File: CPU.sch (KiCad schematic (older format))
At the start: 14 parts, among them J101 Conn_02x10_Odd_Even, J102 Conn_02x14_Odd_Even_MountingP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, Q101 IRLML0040TR, Q102 IRLML0040TR, Q103 DMC4050, SW101 SW_SPDT, U101 ATtiny85-20PU

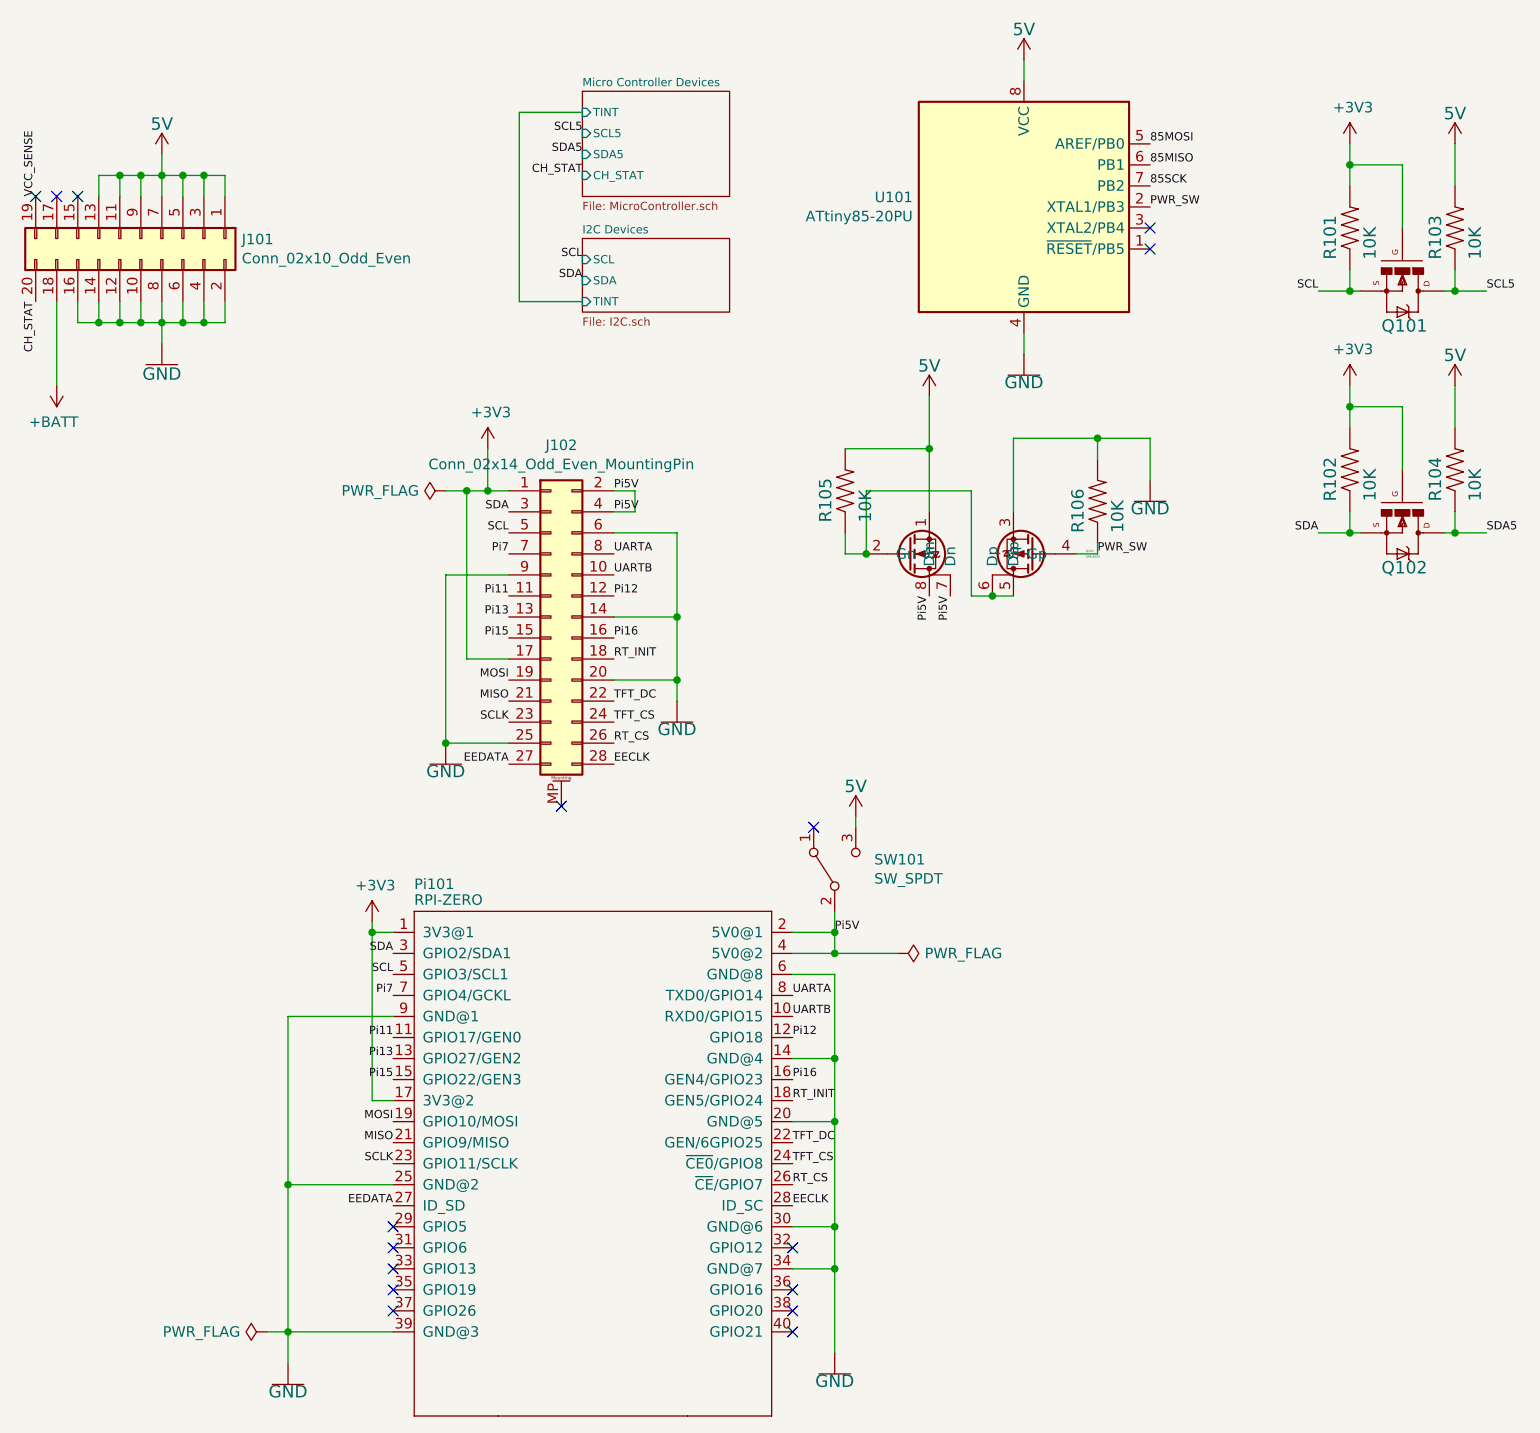
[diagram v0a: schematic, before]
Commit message: Last version before switching to resistive model to read the scroll wheel.
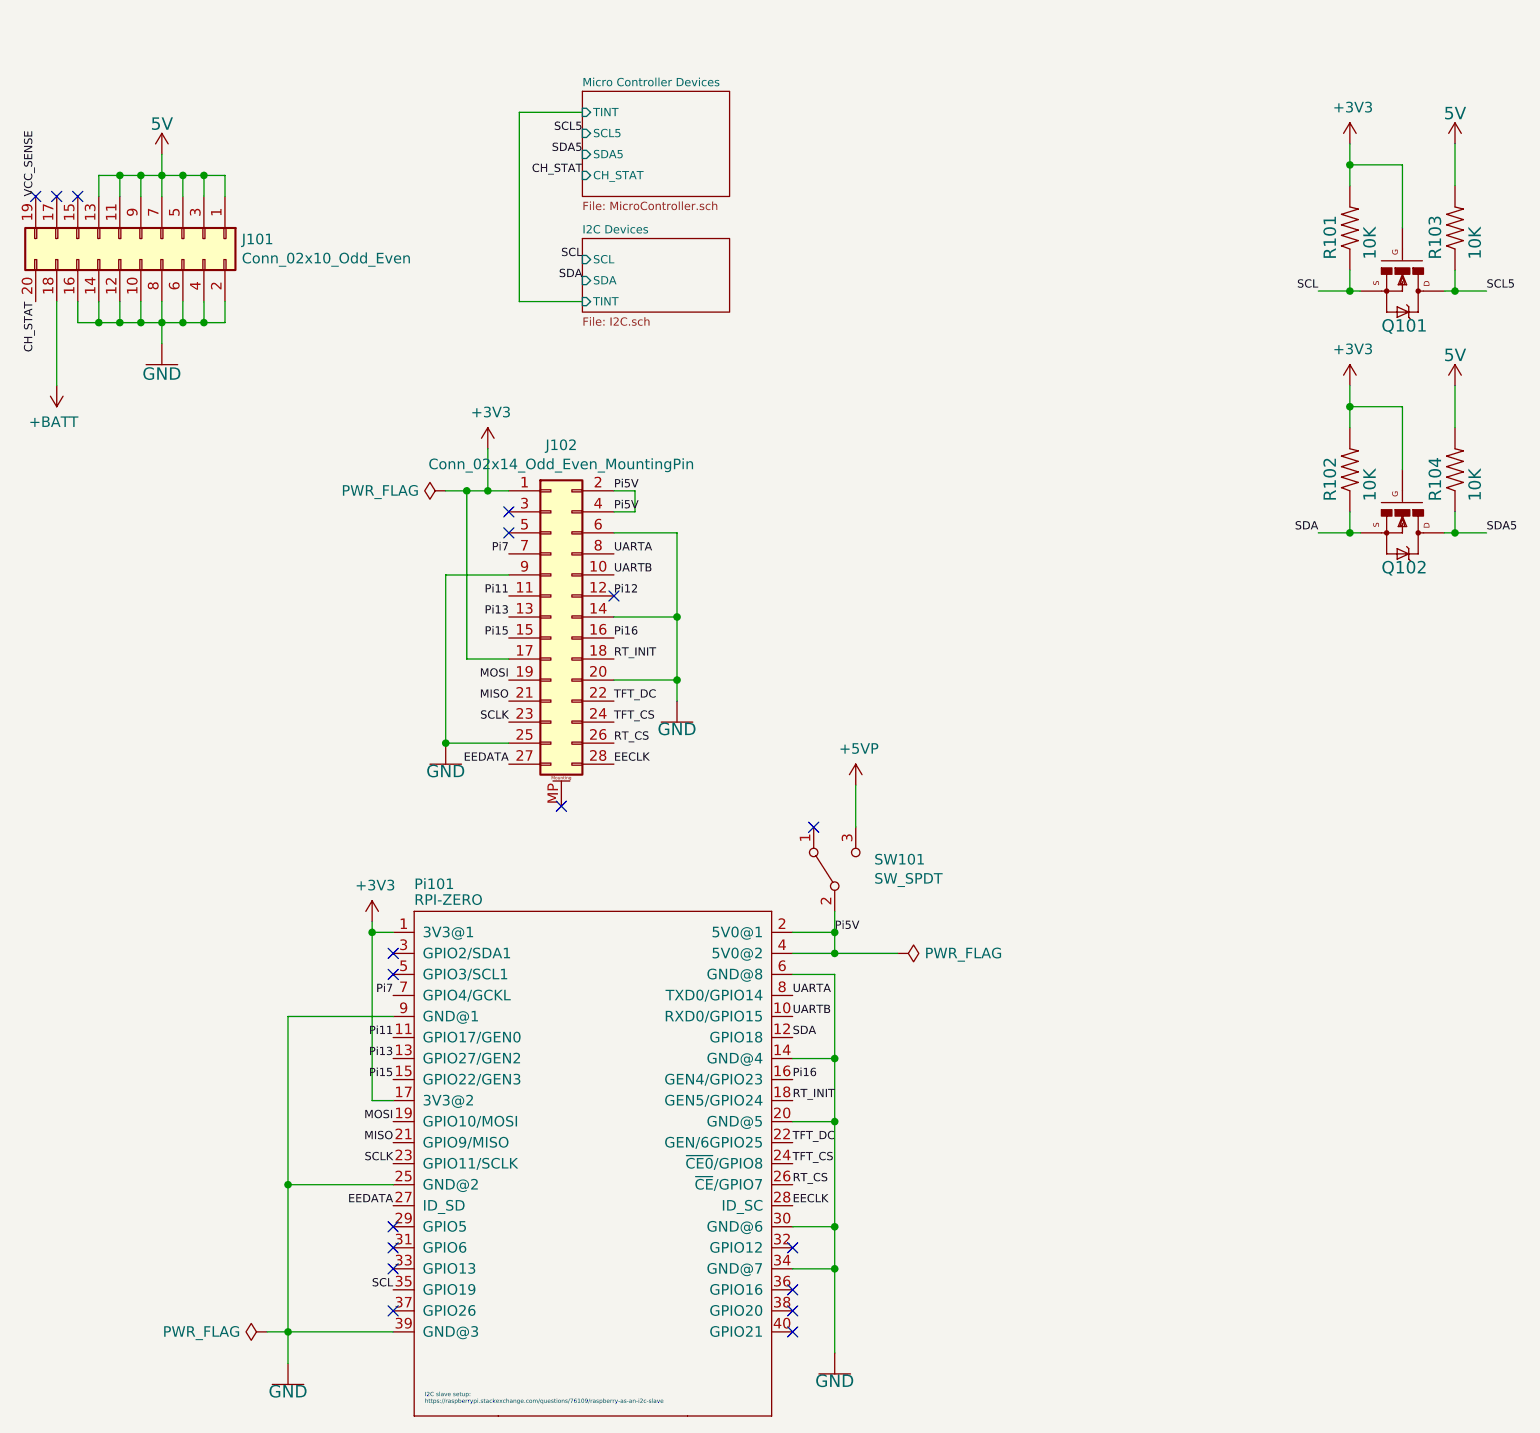
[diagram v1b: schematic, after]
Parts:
- removed Q103: DMC4050, Marco:8-SMD, symbol Marco:DMC4050
- removed R105, R106: 10K, CPU:R1206, symbol CPU-eagle-import:R-US_R1206
- removed U101: ATtiny85-20PU, Marco:8-SMD, symbol MCU_Microchip_ATtiny:ATtiny85-20PU
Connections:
- net Pi12: no longer Pi101.12 (GPIO18)
- net SCL: now also Pi101.35 (GPIO19); no longer J102.5 (Pin_5), Pi101.5 (GPIO3/SCL1)
- net SDA: now also Pi101.12 (GPIO18); no longer J102.3 (Pin_3), Pi101.3 (GPIO2/SDA1)
- net +5VP: now reaches SW101.3 (C)
- no-connect marks 16 -> 18
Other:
- note added: "I2C slave setup:\nhttps://raspberrypi.stackexchange.com/questions/76109/raspberry-as-an-i2c-slave"
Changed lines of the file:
@@
 	5150 5200 5150 5600
 Connection ~ 5150 5600
-$Comp
-L CPU-eagle-import:5V #SUPPLY0102
-U 1 1 5E9EAA7D
-P 5250 4450
-F 0 "#SUPPLY0102" H 5250 4450 50  0001 C CNN
-F 1 "5V" H 5250 4560 59  0000 C BNN
-F 2 "" H 5250 4450 50  0001 C CNN
-F 3 "" H 5250 4450 50  0001 C CNN
-	1    5250 4450
-	1    0    0    -1
-$EndComp
 Wire Wire Line
 	4950 5000 5150 5000
@@
 Text Label 4950 5800 0    39   ~ 0
 RT_INIT
-Text Label 4950 5500 0    39   ~ 0
-Pi12
 $Comp
 L Connector_Generic_MountingPin:Conn_02x14_Odd_Even_MountingPin J102
@@
 	3500 2900 3400 2900
 Connection ~ 3500 2900
-Text Label 3600 3000 2    39   ~ 0
-SDA
-Text Label 3600 3100 2    39   ~ 0
-SCL
 Text Label 3600 3200 2    39   ~ 0
 Pi7
@@
 	5150 5000 5150 4900
 Connection ~ 5150 5000
-Wire Wire Line
-	5250 4500 5250 4450
 Text Label 5150 5000 0    39   ~ 0
 Pi5V
@@
 NoConn ~ 3050 6500
 NoConn ~ 3050 6600
-NoConn ~ 3050 6700
 NoConn ~ 4950 6700
 NoConn ~ 4950 6500
@@
 Text Label 8250 1950 0    39   ~ 0
 SCL5
-Text Label 3050 5100 2    39   ~ 0
+Text Label 4950 5500 0    39   ~ 0
 SDA
-Text Label 3050 5200 2    39   ~ 0
+Text Label 3050 6700 2    39   ~ 0
 SCL
 NoConn ~ 1350 1500
@@
 F4 "TINT" I L 3950 2000 39
 $EndSheet
-$Comp
-L Marco:DMC4050 Q103
-U 1 1 5E925B34
-P 5800 3200
-F 0 "Q103" H 5256 3186 10  0000 R CNN
-F 1 "DMC4050" H 5256 3213 10  0000 R CNN
-F 2 "Marco:8-SMD" H 5800 3200 10  0001 C CNN
-F 3 "" H 5800 3200 10  0001 C CNN
-F 4 "DMC4050SSD-13" H 5800 3200 50  0001 C CNN "DigiKey"
-	1    5800 3200
-	-1   0    0    1
-$EndComp
-$Comp
-L CPU-eagle-import:R-US_R1206 R?
-U 1 1 5E928908
-P 5200 2900
-AR Path="/5E916134/5E928908" Ref="R?"  Part="1"
-AR Path="/5E928908" Ref="R105"  Part="1"
-F 0 "R105" H 5050 2959 59  0000 L BNN
-F 1 "10K" H 5050 2770 59  0000 L BNN
-F 2 "CPU:R1206" H 5200 2900 50  0001 C CNN
-F 3 "" H 5200 2900 50  0001 C CNN
-F 4 " C17902" H 5200 2900 50  0001 C CNN "LCSC Part Number"
-F 5 "RC1206FR-0710KL" H 5200 2900 50  0001 C CNN "DigiKey"
-	1    5200 2900
-	0    -1   -1   0
-$EndComp
-$Comp
-L CPU-eagle-import:R-US_R1206 R?
-U 1 1 5E92C0F5
-P 6400 2950
-AR Path="/5E916134/5E92C0F5" Ref="R?"  Part="1"
-AR Path="/5E92C0F5" Ref="R106"  Part="1"
-F 0 "R106" H 6250 3009 59  0000 L BNN
-F 1 "10K" H 6250 2820 59  0000 L BNN
-F 2 "CPU:R1206" H 6400 2950 50  0001 C CNN
-F 3 "" H 6400 2950 50  0001 C CNN
-F 4 " C17902" H 6400 2950 50  0001 C CNN "LCSC Part Number"
-F 5 "RC1206FR-0710KL" H 6400 2950 50  0001 C CNN "DigiKey"
-	1    6400 2950
-	0    -1   -1   0
-$EndComp
-$Comp
-L CPU-eagle-import:5V #SUPPLY0105
-U 1 1 5E92CA3A
-P 5600 2450
-F 0 "#SUPPLY0105" H 5600 2450 50  0001 C CNN
-F 1 "5V" H 5600 2560 59  0000 C BNN
-F 2 "" H 5600 2450 50  0001 C CNN
-F 3 "" H 5600 2450 50  0001 C CNN
-	1    5600 2450
-	1    0    0    -1
-$EndComp
-Wire Wire Line
-	5200 2700 5600 2700
-Wire Wire Line
-	5600 2700 5600 2450
-Wire Wire Line
-	5600 2700 5600 3000
-Connection ~ 5600 2700
-Wire Wire Line
-	5200 3100 5200 3200
-Wire Wire Line
-	5200 3200 5300 3200
-Wire Wire Line
-	6000 3000 6000 2650
-Wire Wire Line
-	6000 2650 6400 2650
-Wire Wire Line
-	6400 2650 6400 2750
-Wire Wire Line
-	6400 3150 6400 3200
-Wire Wire Line
-	6400 3200 6300 3200
-Wire Wire Line
-	5300 3200 5300 2900
-Wire Wire Line
-	5300 2900 5800 2900
-Wire Wire Line
-	5800 2900 5800 3400
-Wire Wire Line
-	5800 3400 5900 3400
-Connection ~ 5300 3200
-Wire Wire Line
-	6000 3400 5900 3400
-Connection ~ 5900 3400
-Text Label 5600 3400 3    39   ~ 0
-Pi5V
-Text Label 5700 3400 3    39   ~ 0
-Pi5V
-$Comp
-L CPU-eagle-import:GND #GND0106
-U 1 1 5E942D3F
-P 6650 2950
-F 0 "#GND0106" H 6650 2950 50  0001 C CNN
-F 1 "GND" H 6650 2950 59  0000 C TNN
-F 2 "" H 6650 2950 50  0001 C CNN
-F 3 "" H 6650 2950 50  0001 C CNN
-	1    6650 2950
-	1    0    0    -1
-$EndComp
-Wire Wire Line
-	6400 2650 6650 2650
-Wire Wire Line
-	6650 2650 6650 2850
-Connection ~ 6400 2650
-$Comp
-L MCU_Microchip_ATtiny:ATtiny85-20PU U101
-U 1 1 5E9473CE
-P 6050 1550
-F 0 "U101" H 5521 1596 50  0000 R CNN
-F 1 "ATtiny85-20PU" H 5521 1505 50  0000 R CNN
-F 2 "Marco:8-SMD" H 6050 1550 50  0001 C CIN
-F 3 "http://ww1.microchip.com/downloads/en/DeviceDoc/atmel-2586-avr-8-bit-microcontroller-attiny25-attiny45-attiny85_datasheet.pdf" H 6050 1550 50  0001 C CNN
-F 4 "ATTINY85-20SHR" H 6050 1550 50  0001 C CNN "DigiKey"
-	1    6050 1550
-	1    0    0    -1
-$EndComp
-Text Label 6400 3200 0    39   ~ 0
-PWR_SW
-Text Label 6650 1550 0    39   ~ 0
-PWR_SW
-$Comp
-L CPU-eagle-import:5V #SUPPLY?
-U 1 1 5E95C85A
-P 6050 850
-F 0 "#SUPPLY?" H 6050 850 50  0001 C CNN
-F 1 "5V" H 6050 960 59  0000 C BNN
-F 2 "" H 6050 850 50  0001 C CNN
-F 3 "" H 6050 850 50  0001 C CNN
-	1    6050 850
-	1    0    0    -1
-$EndComp
-$Comp
-L CPU-eagle-import:GND #GND?
-U 1 1 5E95CCF7
-P 6050 2350
-F 0 "#GND?" H 6050 2350 50  0001 C CNN
-F 1 "GND" H 6050 2350 59  0000 C TNN
-F 2 "" H 6050 2350 50  0001 C CNN
-F 3 "" H 6050 2350 50  0001 C CNN
-	1    6050 2350
-	1    0    0    -1
-$EndComp
-Wire Wire Line
-	6050 2250 6050 2150
-Wire Wire Line
-	6050 950  6050 850
-NoConn ~ 6650 1750
-NoConn ~ 6650 1650
-Text Label 6650 1450 0    39   ~ 0
-85SCK
-Text Label 6650 1350 0    39   ~ 0
-85MISO
-Text Label 6650 1250 0    39   ~ 0
-85MOSI
+Text Notes 3200 7250 0    20   ~ 0
+I2C slave setup:\nhttps://raspberrypi.stackexchange.com/questions/76109/raspberry-as-an-i2c-slave
+NoConn ~ 4100 3400
+NoConn ~ 3600 3100
+NoConn ~ 3600 3000
+NoConn ~ 3050 5100
+NoConn ~ 3050 5200
+$Comp
+L power:+5VP #PWR0108
+U 1 1 5EB8BD82
+P 5250 4300
+F 0 "#PWR0108" H 5250 4150 50  0001 C CNN
+F 1 "+5VP" H 5265 4473 50  0000 C CNN
+F 2 "" H 5250 4300 50  0001 C CNN
+F 3 "" H 5250 4300 50  0001 C CNN
+	1    5250 4300
+	1    0    0    -1
+$EndComp
+Wire Wire Line
+	5250 4300 5250 4500
 $EndSCHEMATC

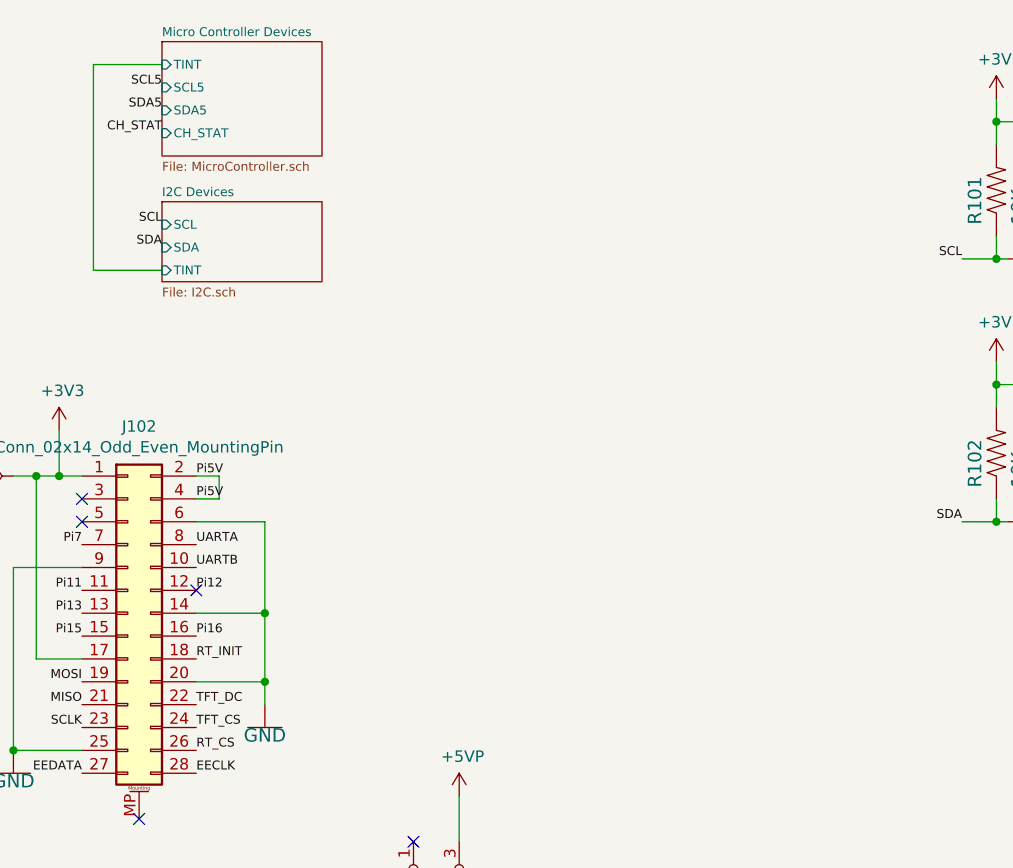
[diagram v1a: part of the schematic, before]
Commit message: Version 2, DRC and ERC clear, ready to send, waiting on V1 to see what did not work.
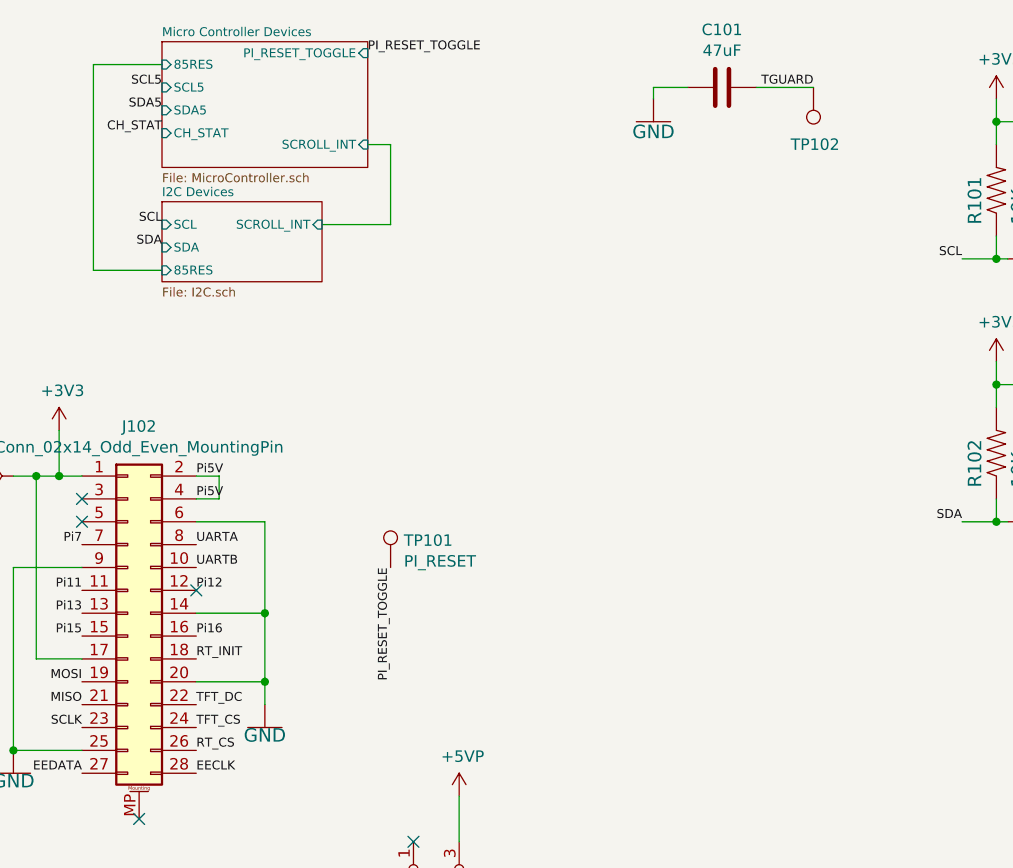
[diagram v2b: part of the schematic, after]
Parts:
- added C101: 47uF, Capacitor_SMD:C_0805_2012Metric_Pad1.15x1.40mm_HandSolder, symbol Device:C
- added TP101: PI_RESET, TestPoint:TestPoint_Pad_D1.0mm, symbol Connector:TestPoint
- added TP102: TestPoint, TestPoint:TestPoint_Pad_D1.0mm, symbol Connector:TestPoint
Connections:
- new net PI_RESET_TOGGLE: TP101.1
- new net TGUARD: C101.2, TP102.1
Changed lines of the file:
@@
 NoConn ~ 3050 6800
 $Sheet
-S 3950 1000 700  500
+S 3950 1000 900  550
 U 5E9D5ED5
 F0 "Micro Controller Devices" 39
@@
 F2 "SDA5" I L 3950 1300 39
 F3 "SCL5" I L 3950 1200 39
-F4 "TINT" I L 3950 1100 39
+F4 "85RES" I L 3950 1100 39
 F5 "CH_STAT" I L 3950 1400 39
+F6 "SCROLL_INT" I R 4850 1450 39
+F7 "PI_RESET_TOGGLE" I R 4850 1050 39
 $EndSheet
 $Comp
@@
 F2 "SCL" I L 3950 1800 39
 F3 "SDA" I L 3950 1900 39
-F4 "TINT" I L 3950 2000 39
+F4 "85RES" I L 3950 2000 39
+F5 "SCROLL_INT" I R 4650 1800 39
 $EndSheet
 Text Notes 3200 7250 0    20   ~ 0
@@
 Wire Wire Line
 	5250 4300 5250 4500
+$Comp
+L Connector:TestPoint TP102
+U 1 1 5EA4DCF3
+P 6800 1200
+AR Path="/5EA4DCF3" Ref="TP102"  Part="1"
+AR Path="/5E916134/5EA4DCF3" Ref="TP?"  Part="1"
+AR Path="/5E9D5ED5/5EA4DCF3" Ref="TP?"  Part="1"
+F 0 "TP102" H 6900 1450 50  0000 R CNN
+F 1 "TestPoint" H 6742 1317 50  0001 R CNN
+F 2 "TestPoint:TestPoint_Pad_D1.0mm" H 7000 1200 50  0001 C CNN
+F 3 "~" H 7000 1200 50  0001 C CNN
+	1    6800 1200
+	-1   0    0    1
+$EndComp
+Text Label 6800 1200 2    39   ~ 0
+TGUARD
+$Comp
+L Device:C C101
+U 1 1 5EA4DCFC
+P 6400 1200
+AR Path="/5EA4DCFC" Ref="C101"  Part="1"
+AR Path="/5E916134/5EA4DCFC" Ref="C?"  Part="1"
+F 0 "C101" V 6652 1200 50  0000 C CNN
+F 1 "47uF" V 6561 1200 50  0000 C CNN
+F 2 "Capacitor_SMD:C_0805_2012Metric_Pad1.15x1.40mm_HandSolder" H 6438 1050 50  0001 C CNN
+F 3 "~" H 6400 1200 50  0001 C CNN
+F 4 " C28323" H 6400 1200 50  0001 C CNN "LCSC Part Number"
+F 5 "C0805C105K3RACTU" H 6400 1200 50  0001 C CNN "DigiKey"
+	1    6400 1200
+	0    -1   -1   0
+$EndComp
+$Comp
+L CPU-eagle-import:GND #GND0106
+U 1 1 5EA4DD02
+P 6100 1350
+AR Path="/5EA4DD02" Ref="#GND0106"  Part="1"
+AR Path="/5E916134/5EA4DD02" Ref="#GND?"  Part="1"
+F 0 "#GND0106" H 6100 1350 50  0001 C CNN
+F 1 "GND" H 6100 1340 59  0000 C TNN
+F 2 "" H 6100 1350 50  0001 C CNN
+F 3 "" H 6100 1350 50  0001 C CNN
+	1    6100 1350
+	1    0    0    -1
+$EndComp
+Wire Wire Line
+	6100 1250 6100 1200
+Wire Wire Line
+	6100 1200 6250 1200
+Wire Wire Line
+	6550 1200 6800 1200
+Wire Wire Line
+	4850 1450 4950 1450
+Wire Wire Line
+	4950 1450 4950 1800
+Wire Wire Line
+	4650 1800 4950 1800
+$Comp
+L Connector:TestPoint TP101
+U 1 1 5EA23027
+P 4950 3300
+F 0 "TP101" H 5008 3418 50  0000 L CNN
+F 1 "PI_RESET" H 5008 3327 50  0000 L CNN
+F 2 "TestPoint:TestPoint_Pad_D1.0mm" H 5150 3300 50  0001 C CNN
+F 3 "~" H 5150 3300 50  0001 C CNN
+	1    4950 3300
+	1    0    0    -1
+$EndComp
+Text Label 4950 3300 3    39   ~ 0
+PI_RESET_TOGGLE
+Text Label 4850 1050 0    39   ~ 0
+PI_RESET_TOGGLE
 $EndSCHEMATC
